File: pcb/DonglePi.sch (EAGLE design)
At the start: 8 parts, among them IC1 MCP1703DB

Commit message: routed the mains
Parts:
- removed GPIO_HEADER1: RPI_GPIO_HEADER, rpi-header:RPI_GPIO_HEADER
- added SWCLK_DBG, SWDIO_DBG: (no value), wirepad:1,6/0,8
- added U$2: RPI_2X13, gbin:RPI_2X13
- R1: value (none) -> 500
- renumbered U$1 to MCU
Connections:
- new net PA00: MCU.PA00, U$2.GPIO17
- new net PA01: MCU.PA01, U$2.GPIO22
- new net PA02: MCU.PA02, U$2.GPIO07
- new net PA03: MCU.PA03
- new net PA04: MCU.PA04, U$2.GPIO18
- new net PA05: MCU.PA05, U$2.GPIO23
- new net PA06: MCU.PA06, U$2.GPIO27
- new net PA07: MCU.PA07, U$2.GPIO24
- new net PA08: MCU.PA08, U$2.GPIO10
- new net PA09: MCU.PA09, U$2.GPIO09
- new net PA10: MCU.PA10, U$2.GPIO11
- new net PA11: MCU.PA11, U$2.GPIO08
- new net PA14: MCU.PA14, U$2.GPIO14
- new net PA15: MCU.PA15, U$2.GPIO15
- new net PA16: MCU.PA16, U$2.GPIO02
- new net PA17: MCU.PA17, U$2.GPIO03
- new net PA18: MCU.PA18
- new net PA19: MCU.PA19
- new net PA22: MCU.PA22, U$2.GPIO04
- new net PA23: MCU.PA23, U$2.GPIO25
- new net PA24: MCU.PA24, X1.2
- new net PA25: MCU.PA25, X1.3
- new net PA27: MCU.PA27
- new net PA30: MCU.PA30, SWCLK_DBG.P
- new net PA31: MCU.PA31, SWDIO_DBG.P
- net +3V3: now also U$2.3.3V
- net +5V: now also U$2.5V, U$2.5V_2
- net GND: now also U$2.3.3V_2, U$2.GND, U$2.GND_2, U$2.GND_3, U$2.GND_4, U$2.GND_5

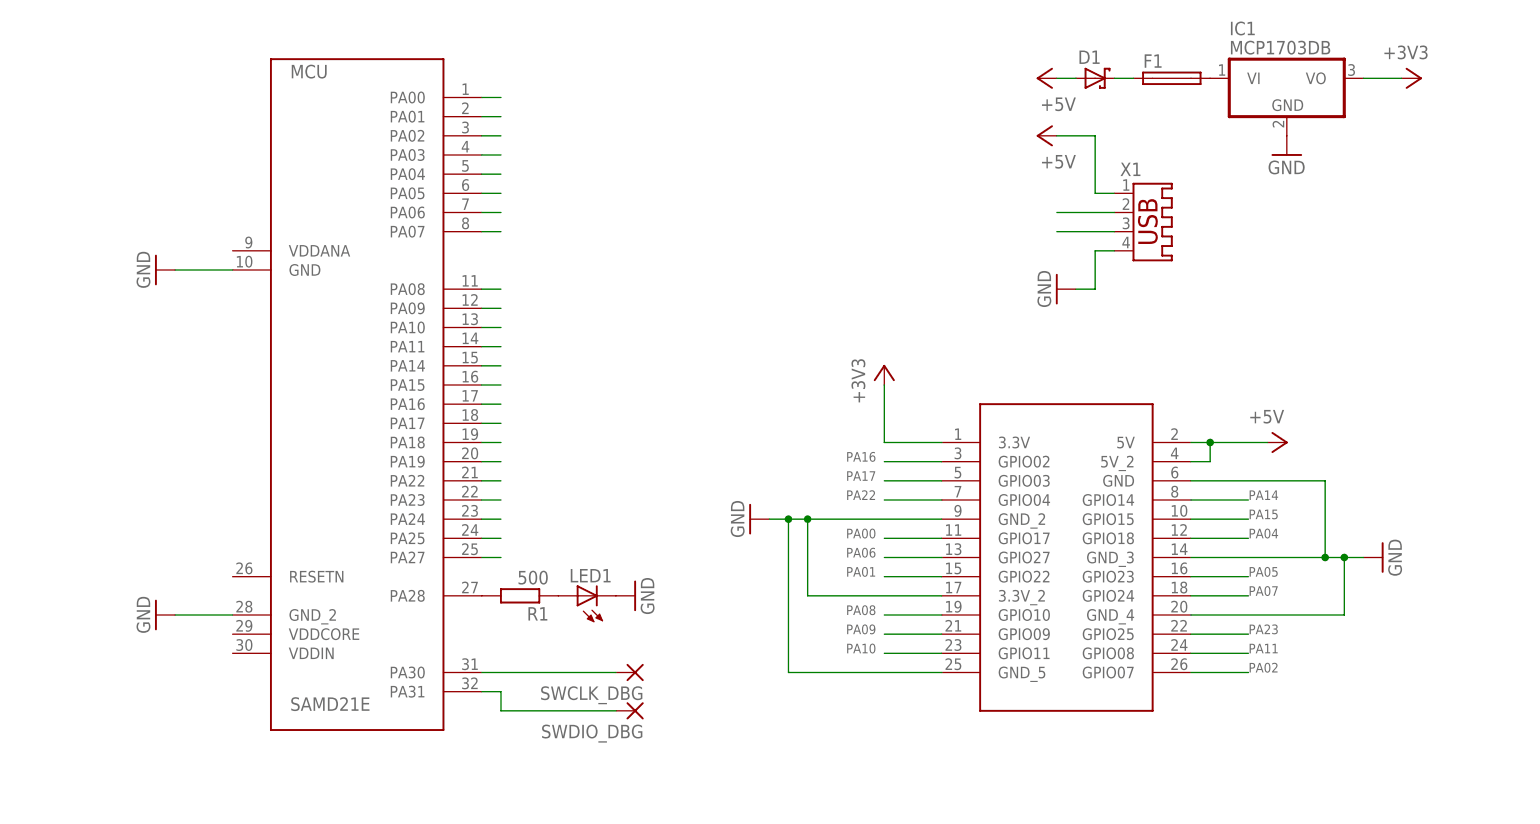
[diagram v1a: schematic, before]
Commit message: Better components, noise protection.
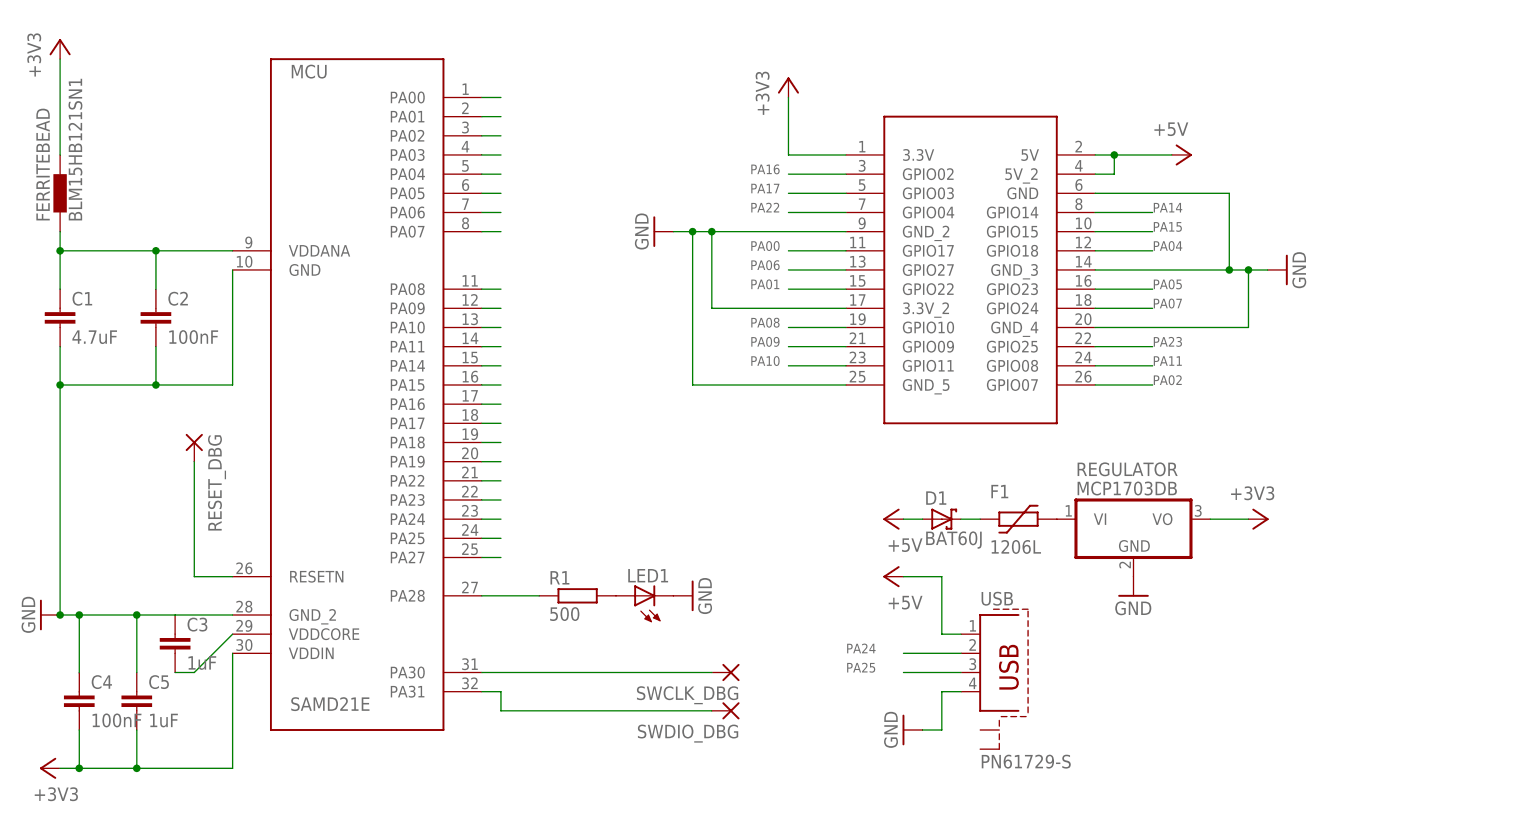
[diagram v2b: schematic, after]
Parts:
- removed IC1: MCP1703DB, linear:MCP1703DB
- removed X1: (no value), con-yamaichi:USB-A003
- added C1: 4.7uF, eagle-ltspice:CC0504
- added C2, C4: 100nF, eagle-ltspice:CC0504
- added C3, C5: 1uF, eagle-ltspice:CC0504
- added FERRITEBEAD: BLM15HB121SN1, inductors:BLM15HB121SN1
- added REGULATOR: MCP1703DB, linear:MCP1703DB
- added RESET_DBG: (no value), wirepad:1,6/0,8
- added USB: PN61729-S, con-berg:PN61729-S
- D1: value (none) -> BAT60J; device diode:SCHOTTKY-DIODESMD -> diode:BAT60J
- F1: value (none) -> 1206L; device fuse:TE5 -> gbin:1206L
- R1: device eagle-ltspice:RR3216 -> rcl:R-EU_M0805
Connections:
- new net N$3: MCU.PA28, R1.1
- new net N$6: C3.2, MCU.VDDCORE
- new net N$7: MCU.RESETN, RESET_DBG.P
- net +3V3: now also C4.2, C5.2, FERRITEBEAD.2, MCU.VDDIN, REGULATOR.VO; no longer IC1.VO
- net +5V: now also USB.1; no longer X1.1
- net GND: now also C1.2, C2.2, C3.1, C4.1, C5.1, REGULATOR.GND, USB.4; no longer IC1.GND, X1.4
- net N$1: now also REGULATOR.VI; no longer IC1.VI
- net N$4: now also R1.2; no longer R1.1
- net N$5: now also C1.1, C2.1, FERRITEBEAD.1, MCU.VDDANA; no longer MCU.PA28, R1.2
- net PA24: now also USB.2; no longer X1.2
- net PA25: now also USB.3; no longer X1.3
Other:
- moved on the sheet: D1, LED1, R1, SWCLK_DBG, SWDIO_DBG

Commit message: pass on sch
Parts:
- removed U$2: RPI_2X13, gbin:RPI_2X13
- removed USB: PN61729-S, con-berg:PN61729-S
- added LED2: _, eagle-ltspice:LED_ESML0603
- added PA18_GPIO, PA19_GPIO, PA27_GPIO: _, wirepad:1,6/0,8
- added R2: 500, eagle-ltspice:RR0201
- added RPIO: RPI_2X13, gbin:RPI_2X13
- added USB_MALE: USB-A-H, gbin:USB-A-H
- LED1, RESET_DBG, SWCLK_DBG, SWDIO_DBG: value (none) -> _
- R1: device rcl:R-EU_M0805 -> eagle-ltspice:RR0201
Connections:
- new net N$6: LED2.A, R2.2
- net +3V3: now also RPIO.3.3V; no longer U$2.3.3V
- net +5V: now also RPIO.5V, RPIO.5V_2, USB_MALE.VBUS; no longer U$2.5V, U$2.5V_2, USB.1
- net GND: now also LED2.C, RPIO.3.3V_2, RPIO.GND, RPIO.GND_2, RPIO.GND_3, RPIO.GND_4, RPIO.GND_5, USB_MALE.GND; no longer U$2.3.3V_2, U$2.GND, U$2.GND_2, U$2.GND_3, U$2.GND_4, U$2.GND_5, USB.4
- net PA00: now also RPIO.GPIO17; no longer U$2.GPIO17
- net PA01: now also RPIO.GPIO22; no longer U$2.GPIO22
- net PA02: now also RPIO.GPIO07; no longer U$2.GPIO07
- net PA03: now also R2.1
- net PA04: now also RPIO.GPIO18; no longer U$2.GPIO18
- net PA05: now also RPIO.GPIO23; no longer U$2.GPIO23
- net PA06: now also RPIO.GPIO27; no longer U$2.GPIO27
- net PA07: now also RPIO.GPIO24; no longer U$2.GPIO24
- net PA08: now also RPIO.GPIO10; no longer U$2.GPIO10
- net PA09: now also RPIO.GPIO09; no longer U$2.GPIO09
- net PA10: now also RPIO.GPIO11; no longer U$2.GPIO11
- net PA11: now also RPIO.GPIO08; no longer U$2.GPIO08
- net PA14: now also RPIO.GPIO14; no longer U$2.GPIO14
- net PA15: now also RPIO.GPIO15; no longer U$2.GPIO15
- net PA16: now also RPIO.GPIO02; no longer U$2.GPIO02
- net PA17: now also RPIO.GPIO03; no longer U$2.GPIO03
- net PA18: now also PA18_GPIO.P
- net PA19: now also PA19_GPIO.P
- net PA22: now also RPIO.GPIO04; no longer U$2.GPIO04
- net PA23: now also RPIO.GPIO25; no longer U$2.GPIO25
- net PA24: now also USB_MALE.D-; no longer USB.2
- net PA25: now also USB_MALE.D+; no longer USB.3
- net PA27: now also PA27_GPIO.P
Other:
- moved on the sheet: LED1, R1, SWCLK_DBG, SWDIO_DBG

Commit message: silkscreen / routing POC
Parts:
- removed PA18_GPIO, PA19_GPIO, PA27_GPIO: _, wirepad:1,6/0,8
- renumbered F1 to FUSE
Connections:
- net PA18: no longer PA18_GPIO.P
- net PA19: no longer PA19_GPIO.P
- net PA27: no longer PA27_GPIO.P
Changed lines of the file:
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@@
 </variantdefs>
 <classes>
-<class number="0" name="default" width="0" drill="0">
+<class number="0" name="default" width="0.254" drill="0">
+</class>
+<class number="1" name="3VPower" width="0.3048" drill="0">
+</class>
+<class number="2" name="5V" width="0.3048" drill="0">
+</class>
+<class number="3" name="Ground" width="0.3048" drill="0">
 </class>
 </classes>
@@
 <part name="SWDIO_DBG" library="wirepad" deviceset="1,6/0,8" device="" value="_"/>
 <part name="SWCLK_DBG" library="wirepad" deviceset="1,6/0,8" device="" value="_"/>
-<part name="F1" library="gbin" deviceset="1206L" device=""/>
+<part name="FUSE" library="gbin" deviceset="1206L" device=""/>
 <part name="FERRITEBEAD" library="inductors" deviceset="BLM15H" device="" technology="B121SN1"/>
 <part name="+3V3" library="supply1" deviceset="+3V3" device=""/>
@@
 <part name="LED2" library="eagle-ltspice" deviceset="LED_E" device="SML0603" value="_"/>
 <part name="GND1" library="supply1" deviceset="GND" device=""/>
-<part name="PA18_GPIO" library="wirepad" deviceset="1,6/0,8" device="" value="_"/>
-<part name="PA19_GPIO" library="wirepad" deviceset="1,6/0,8" device="" value="_"/>
-<part name="PA27_GPIO" library="wirepad" deviceset="1,6/0,8" device="" value="_"/>
 </parts>
 <sheets>
@@
 <instance part="SWDIO_DBG" gate="P" x="60.96" y="-10.16" rot="R180"/>
 <instance part="SWCLK_DBG" gate="P" x="60.96" y="-5.08" rot="R180"/>
-<instance part="F1" gate="G$1" x="101.6" y="15.24"/>
+<instance part="FUSE" gate="G$1" x="101.6" y="15.24"/>
 <instance part="FERRITEBEAD" gate="G$1" x="-25.4" y="58.42" rot="R90"/>
 <instance part="+3V3" gate="G$1" x="-25.4" y="78.74"/>
@@
 <instance part="LED2" gate="G$1" x="53.34" y="63.5" rot="R90"/>
 <instance part="GND1" gate="1" x="60.96" y="63.5" rot="R90"/>
-<instance part="PA18_GPIO" gate="P" x="60.96" y="25.4" rot="R180"/>
-<instance part="PA19_GPIO" gate="P" x="60.96" y="20.32" rot="R180"/>
-<instance part="PA27_GPIO" gate="P" x="60.96" y="15.24" rot="R180"/>
 </instances>
 <busses>
 </busses>
 <nets>
-<net name="+3V3" class="0">
+<net name="+3V3" class="1">
 <segment>
 <pinref part="+3V1" gate="G$1" pin="+3V3"/>
@@
 </segment>
 </net>
-<net name="GND" class="0">
+<net name="GND" class="3">
 <segment>
 <pinref part="REGULATOR" gate="G$1" pin="GND"/>
@@
 </segment>
 </net>
-<net name="+5V" class="0">
+<net name="+5V" class="2">
 <segment>
 <pinref part="P+2" gate="1" pin="+5V"/>
@@
 </segment>
 </net>
-<net name="N$2" class="0">
+<net name="N$2" class="2">
 <segment>
 <wire x1="93.98" y1="15.24" x2="96.52" y2="15.24" width="0.1524" layer="91"/>
-<pinref part="F1" gate="G$1" pin="1"/>
+<pinref part="FUSE" gate="G$1" pin="1"/>
 <pinref part="D1" gate="G$1" pin="C"/>
 </segment>
@@
 <segment>
 <pinref part="MCU" gate="SAMD21E" pin="PA18"/>
-<pinref part="PA18_GPIO" gate="P" pin="P"/>
 <wire x1="30.48" y1="25.4" x2="58.42" y2="25.4" width="0.1524" layer="91"/>
 </segment>
@@
 <wire x1="30.48" y1="22.86" x2="48.26" y2="22.86" width="0.1524" layer="91"/>
 <wire x1="48.26" y1="22.86" x2="48.26" y2="20.32" width="0.1524" layer="91"/>
-<pinref part="PA19_GPIO" gate="P" pin="P"/>
 <wire x1="48.26" y1="20.32" x2="58.42" y2="20.32" width="0.1524" layer="91"/>
 </segment>
@@
 <wire x1="30.48" y1="10.16" x2="45.72" y2="10.16" width="0.1524" layer="91"/>
 <wire x1="45.72" y1="10.16" x2="45.72" y2="15.24" width="0.1524" layer="91"/>
-<pinref part="PA27_GPIO" gate="P" pin="P"/>
 <wire x1="45.72" y1="15.24" x2="58.42" y2="15.24" width="0.1524" layer="91"/>
 </segment>
@@
 <segment>
 <pinref part="REGULATOR" gate="G$1" pin="VI"/>
-<pinref part="F1" gate="G$1" pin="2"/>
-</segment>
-</net>
+<pinref part="FUSE" gate="G$1" pin="2"/>
+</segment>
+</net>
